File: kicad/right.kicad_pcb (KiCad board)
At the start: 4 copper layers, 127.3 x 89.6 mm, 131 parts, among them Q1 PMF170XP,115, Q2 FS8205A_C2830320, SW1 TS-1088-AR02016, U1 SN74LVC1G17DBVR, U2 E73-2G4M08S1C, U3 SN74LVC1G74DQER, U4 S2B-PH-K-S(LF)(SN), U5 BL8573CS8TR, U6 DW01A_C42380662, U7 LP5024RSMR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

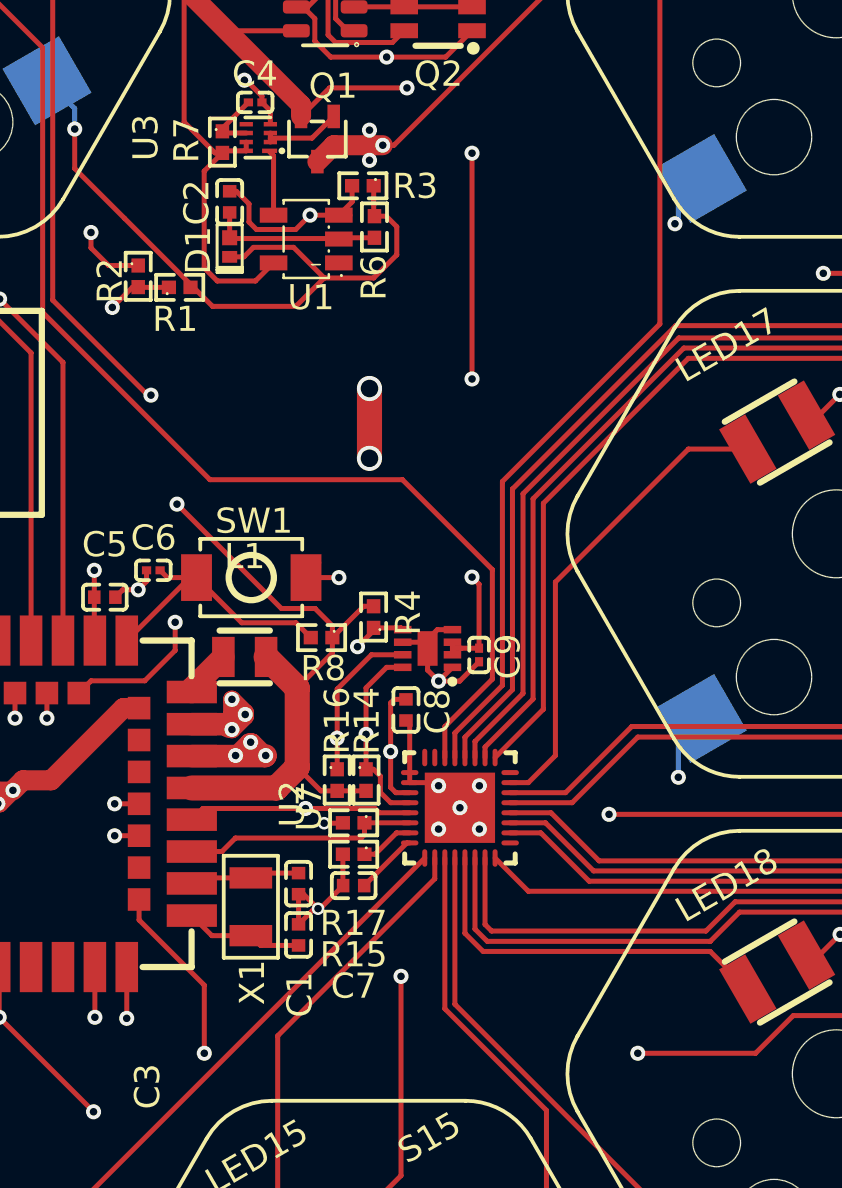
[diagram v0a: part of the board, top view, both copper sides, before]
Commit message: finished. needes inspection. added battery measurer. wired left side
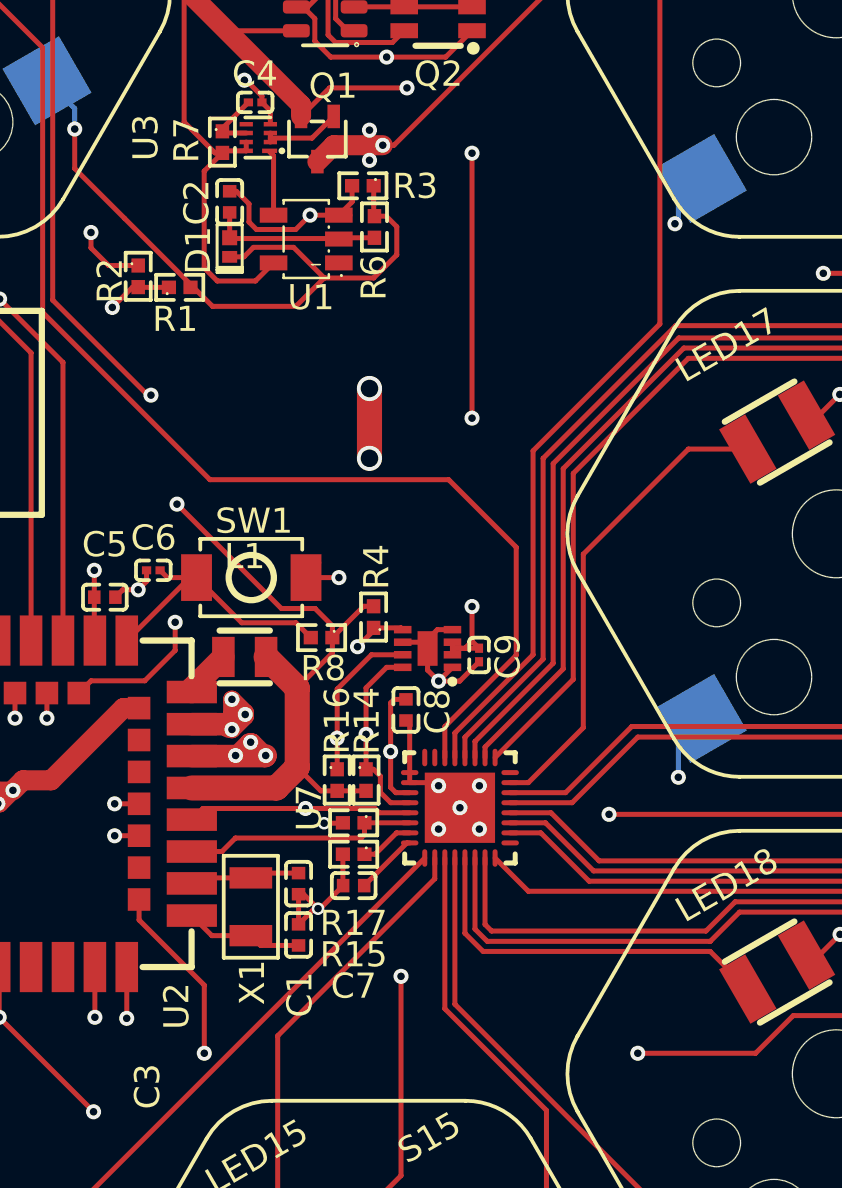
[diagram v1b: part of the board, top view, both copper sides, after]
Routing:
- net /LED20: track 53.5 -> 55.4 mm

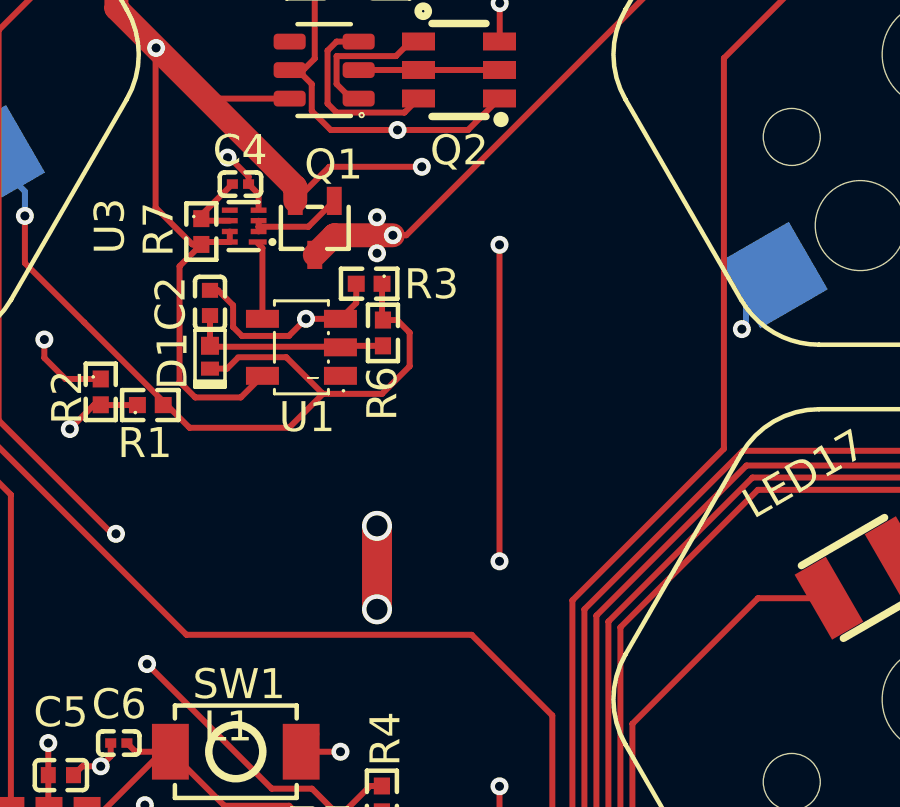
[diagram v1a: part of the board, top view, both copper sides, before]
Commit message: changed on/off timing resistor to 2M61 0805
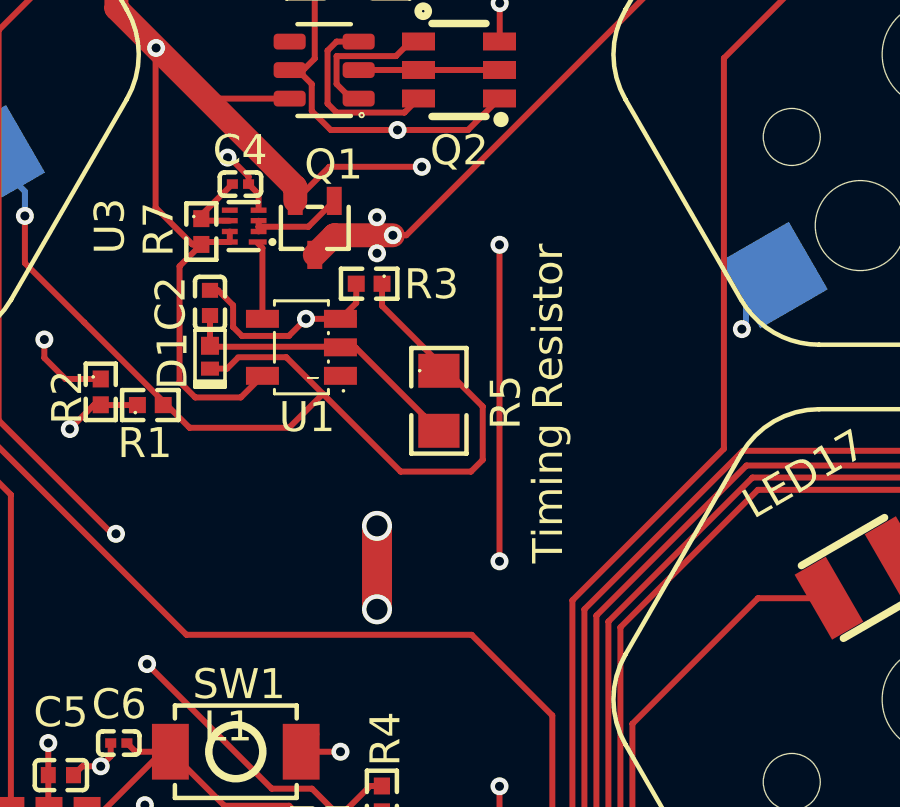
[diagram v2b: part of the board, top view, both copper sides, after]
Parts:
- removed R6: 0402WGF1604TCE, easyeda2kicad:R0402
- added R5: RC0805FR-072M61L, easyeda2kicad:R0805, F.Cu at (69.6, 63.7)
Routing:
- net /PWR_BTN: track 27.7 -> 35.5 mm
- net Net-(U1-A): track 6.51 -> 9.32 mm

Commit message: added gnd vias all over the board. went trough schematic again. changed resistor for rc to bigger one in footprint, and smaller one in Ohm. both left and right sides are ready. just need to go over the kicads check and lastly let someone on discord have a look on the project
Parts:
- removed Fi1, Fi2, Fi3: Fiducial_1mm_Mask2mm, 
- removed G*** (x2): LOGO, images:monster
- removed R15: RT0402BRD0737K4L, easyeda2kicad:R0402
- added BAT+: TestPoint_Pad_D1.5mm, TestPoint:TestPoint_Pad_D1.5mm, F.Cu at (60.3, 40.0)
- added GND: TestPoint_Pad_D1.5mm, TestPoint:TestPoint_Pad_D1.5mm, F.Cu at (57.2, 42.8)
- added PWR: TestPoint_Pad_D1.5mm, TestPoint:TestPoint_Pad_D1.5mm, F.Cu at (69.5, 69.3)
- added R6: ERA2AED753X, easyeda2kicad:R0402, F.Cu at (66.9, 86.4)
- added VBUS: TestPoint_Pad_D1.5mm, TestPoint:TestPoint_Pad_D1.5mm, F.Cu at (74.5, 42.5)
- added VDD_nrf: TestPoint_Pad_D1.5mm, TestPoint:TestPoint_Pad_D1.5mm, F.Cu at (58.6, 71.4)
- G**: moved to B.Cu
- moved G** 281.1 mm to (57.1, 71.6), turned to 180 degrees
- moved Fi4 1.00 mm to (40.4, 52.2)
- moved Fi5 1.00 mm to (169.4, 52.2)
- moved Fi6 1.00 mm to (40.4, 116.6)
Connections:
- U6 pad 5: GND -> /BAT+
- U6 pad 6: /BAT+ -> GND
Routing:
- net /PWR: track 594.8 -> 600.5 mm
- net /VBUS: track 43.9 -> 47.7 mm
- net /BAT+: track 95.0 -> 98.5 mm
- net GND: track 92.3 -> 94.5 mm, vias 31 -> 98
- net /ROW4: track 78.9 -> 80.7 mm
- net /VDD_nRF: track 58.9 -> 60.7 mm
- net /COL1: track 212.8 -> 214.3 mm
- net /COL4: track 172.2 -> 171.1 mm
- net /ROW2: track 131.1 -> 131.9 mm
- net /ROW3: track 149.7 -> 149.2 mm
